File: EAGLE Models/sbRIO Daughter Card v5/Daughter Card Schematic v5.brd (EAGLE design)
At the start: 101.6 x 81.3 mm, 67 parts, among them IC1 BTS716G, IC2 BTS716G, IC3 BTS716G, Q7 MMBT4403-7-F, Q8 MMBT4403-7-F, U2 ADXL345, U3 L3G4200D

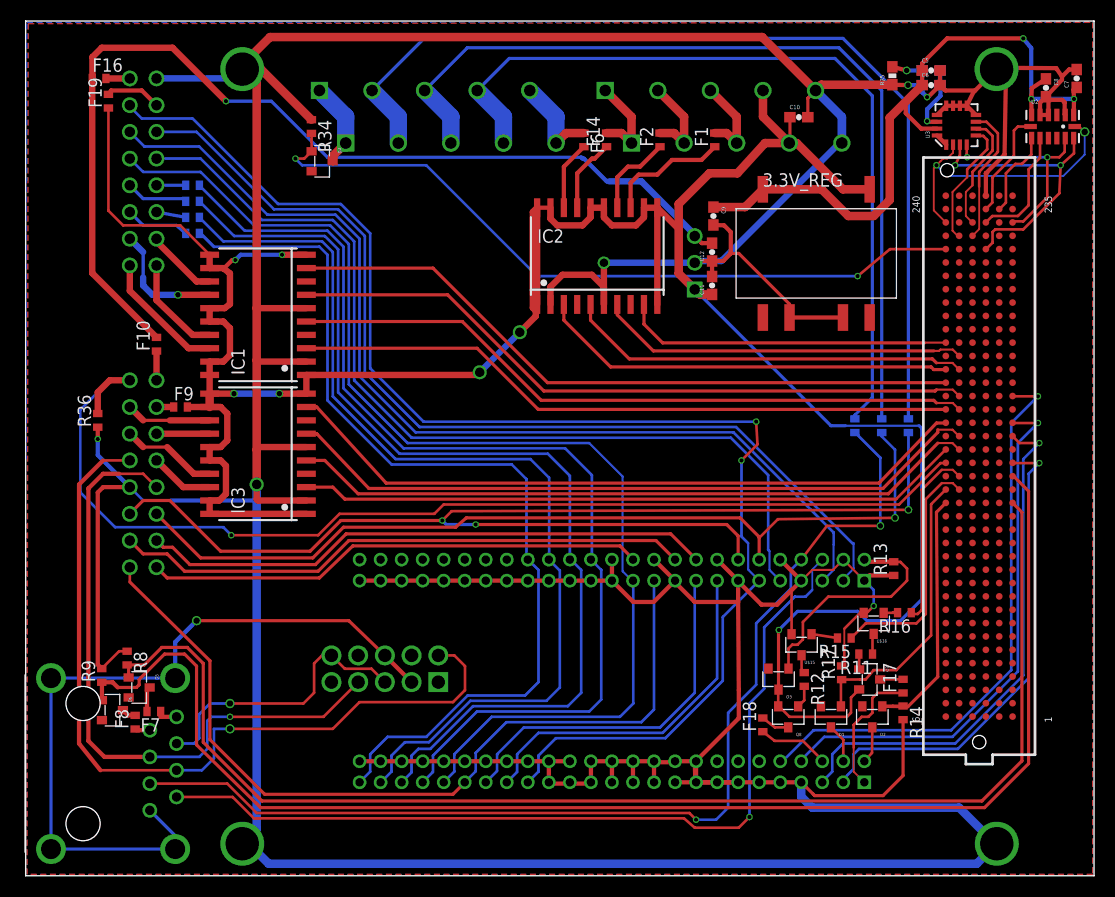
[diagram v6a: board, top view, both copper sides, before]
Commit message: fixing drc errors
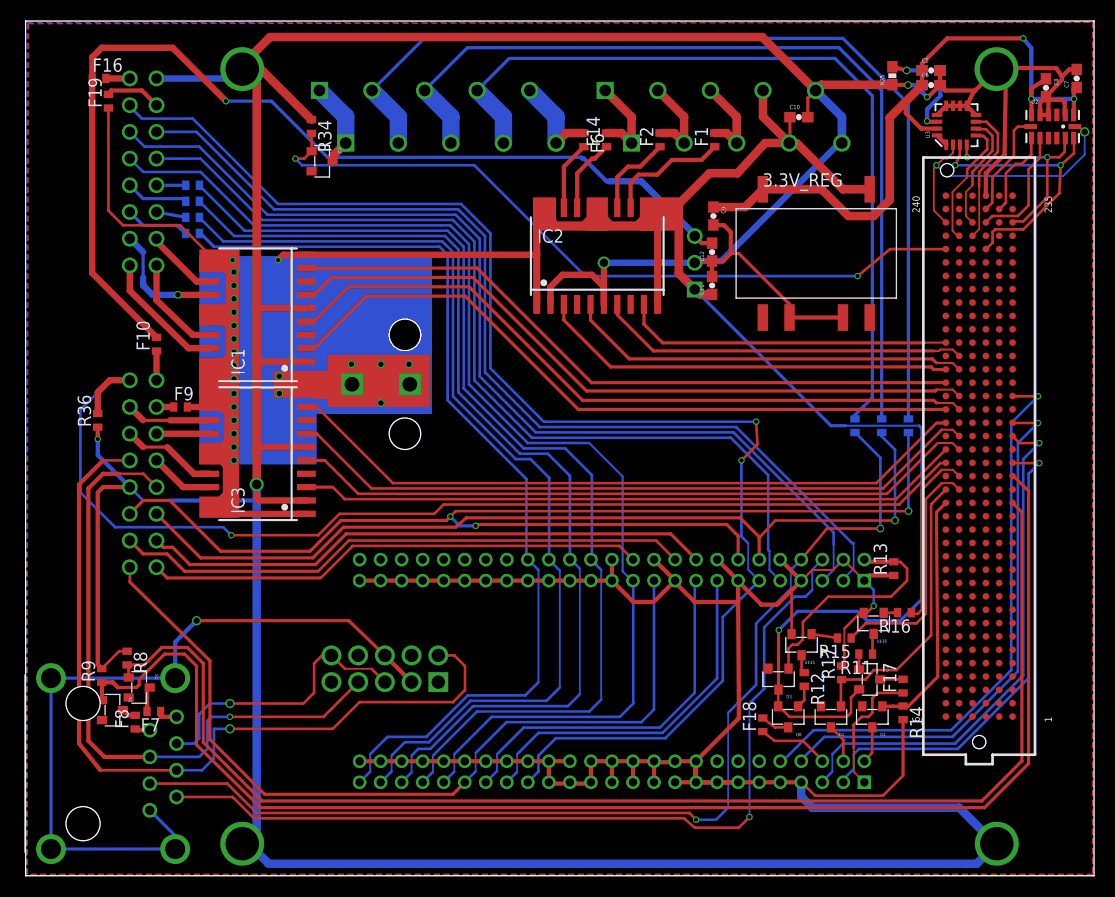
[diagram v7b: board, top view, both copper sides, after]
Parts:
- added X1: 5566-2, con-molex:5566-2
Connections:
- net N$5 renamed VCC
- net 12V: now also X1.1, X1.2
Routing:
- net N$5: track 0.00 -> 11.1 mm
- net 12V: track 282.6 -> 287.2 mm, vias 7 -> 6
- net DIO9: track 63.2 -> 67.3 mm
- net DIO41: track 65.5 -> 68.3 mm
- net DIO40: track 66.2 -> 67.5 mm

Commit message: Added pours and molex connector for amplified 12V
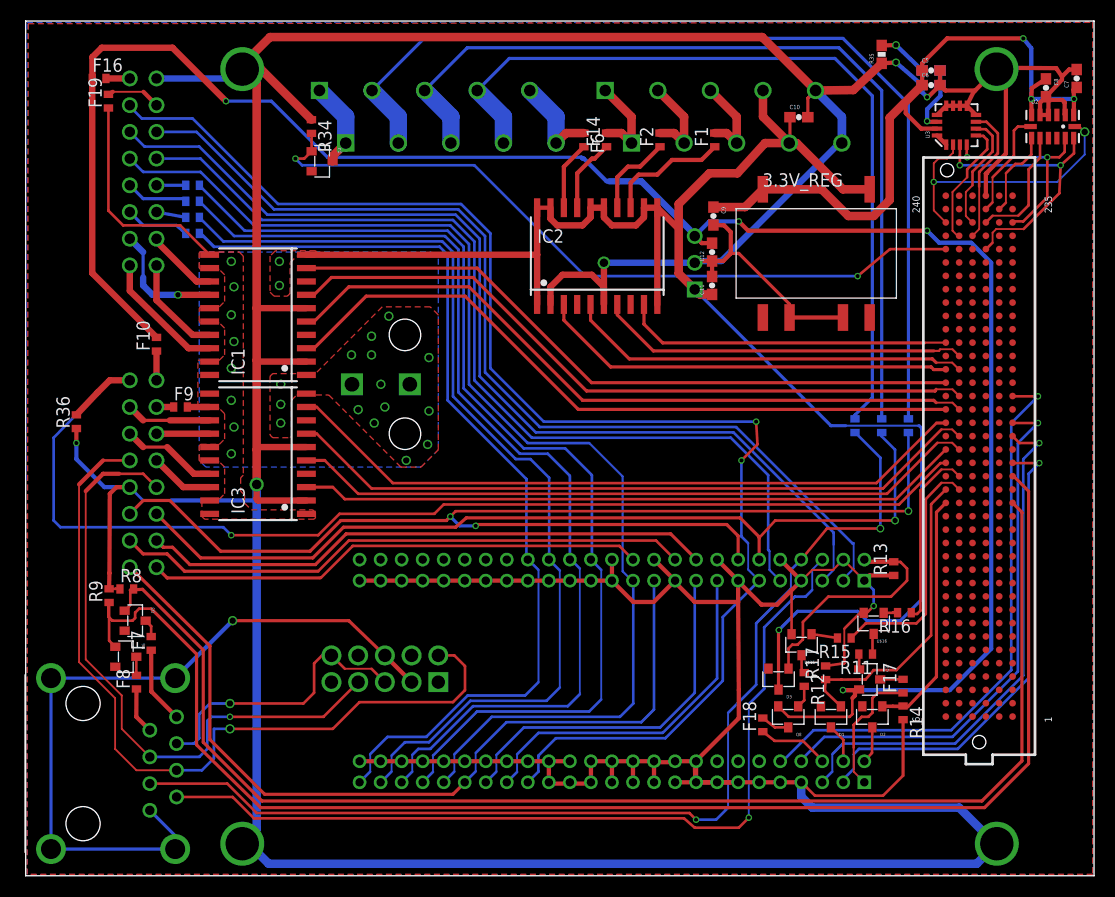
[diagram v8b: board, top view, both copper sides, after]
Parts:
- moved R9 7.62 mm to (7.94, 26.6)
- moved R8 6.57 mm to (9.62, 27.3), turned to 0 degrees
- moved F7 6.48 mm to (11.9, 22.1), turned to 90 degrees
- moved D5 6.36 mm to (10.4, 24.3)
- moved D6 5.24 mm to (9.53, 20.8)
- moved F8 3.81 mm to (10.5, 18.4)
- moved R35 2.27 mm to (81.4, 78.1)
- moved R36 2.04 mm to (4.83, 43.2)
- moved R17 1.52 mm to (76.1, 19.3)
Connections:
- net 12V: no longer Q7.P$3, Q8.P$3
- net 5V: now also Q7.P$3, Q8.P$3
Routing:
- net 5V: track 96.3 -> 191.7 mm, vias 1 -> 4
- net 12V: track 287.2 -> 193.7 mm, vias 6 -> 26
- net N$5: track 11.1 -> 0.00 mm
- net DIO12: track 106.1 -> 112.2 mm
- net GND: track 629.7 -> 623.9 mm
- net N$14: track 2.02 -> 7.32 mm
- net DIO94: track 131.8 -> 136.9 mm
- net DIO95: track 124.0 -> 127.3 mm
- net N$13: track 1.44 -> 4.46 mm
- net CAN_H: track 62.4 -> 60.1 mm
- net DIO13: track 27.3 -> 29.5 mm
- net CAN_GND: track 73.7 -> 71.7 mm
- net N$38: track 2.88 -> 4.83 mm
- net CAN_L: track 78.4 -> 76.5 mm
- net IMD_OK: track 2.39 -> 1.73 mm
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- added copper zone on layer 1, net 12V
- added copper zone on layer 16, net 12V
